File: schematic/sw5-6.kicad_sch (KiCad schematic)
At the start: 2 parts, among them SW5 SW_Push, SW6 SW_Push

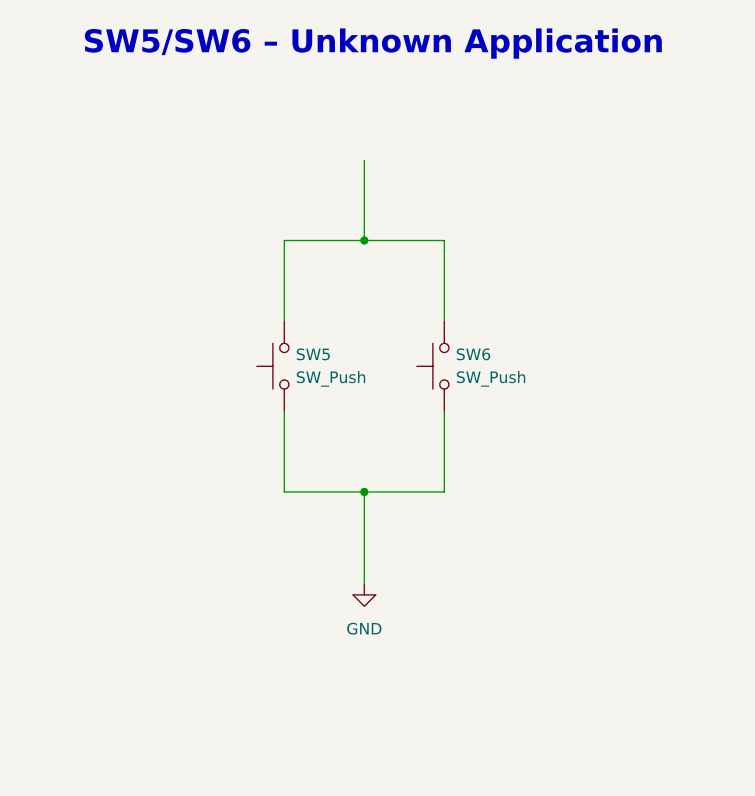
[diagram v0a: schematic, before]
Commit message: Added J5 and assoc. resistor network. Added traceable signals for MYSTERY_SIG
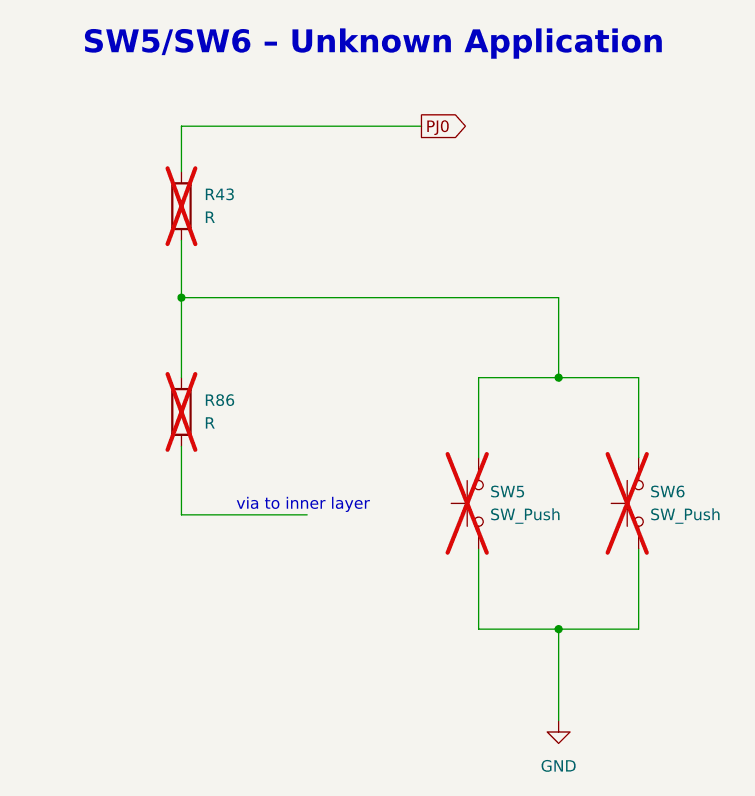
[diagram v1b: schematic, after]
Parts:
- added R43, R86: R, symbol Device:R
- SW5, SW6: now not fitted
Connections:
- net at SW5.2, SW6.2: now also R43.2, R86.1
- new net PJ0: R43.1
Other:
- note added: "via to inner layer"
